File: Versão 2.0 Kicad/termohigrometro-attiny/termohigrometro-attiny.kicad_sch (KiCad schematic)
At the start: 19 parts, among them J1 Conn_02x03_Odd_Even, J3 Chave, J4 Screw_Terminal_01x04, J5 Screw_Terminal_01x04, J6 Carregador, U1 ATtiny85-20P, U2 AMS1117-3.3

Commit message: placa com attiny
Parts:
- added J2: Fan, TerminalBlock_4Ucon:TerminalBlock_4Ucon_1x02_P3.50mm_Horizontal, symbol Connector:Screw_Terminal_01x02
- added Q1: 2N7002K, Package_TO_SOT_SMD:SOT-23, symbol Transistor_FET:2N7002K
- added R1, R4: 1M, Resistor_THT:R_Axial_DIN0207_L6.3mm_D2.5mm_P10.16mm_Horizontal, symbol Device:R
- added R6: 100, Resistor_THT:R_Axial_DIN0207_L6.3mm_D2.5mm_P10.16mm_Horizontal, symbol Device:R
- added R7: 10k, Resistor_SMD:R_0805_2012Metric, symbol Device:R
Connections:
- net +BATT: now also J2.1 (Pin_1), R1.1
- net GND: now also Q1.2 (S), R4.2, R7.1
- net FAN: now reaches U1.2 (XTAL1/PB3)
- net FAN: now also R6.1
- net VBS: now reaches U1.3 (XTAL2/PB4)
- net VBS: now also R1.2, R4.1
- new net: J2.2 (Pin_2), Q1.3 (D)
- new net: Q1.1 (G), R6.2, R7.2
- no-connect marks 2 -> 0
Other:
- note added: "https://mjvo.github.io/tutorials/circuits/attiny85/"
- moved on the sheet: BT1, C7, C8, J3, J6, U2

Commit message: organizando
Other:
- note added: "Bateria"
- note added: "Conectores I2C"
- note added: "Controlador Attiny85"
- note added: "Furos de montagem"
- note added: "Regulador de tensão"
- note added: "Saída a MOSFET"
- note added: "Sensor da bateria"
- company: (none) -> Sentium Controls
- title: (none) -> Termohigrômetro
- moved on the sheet: BT1, C2, C7, C8, C9, D1, H1, H2, H3, J1, J2, J3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

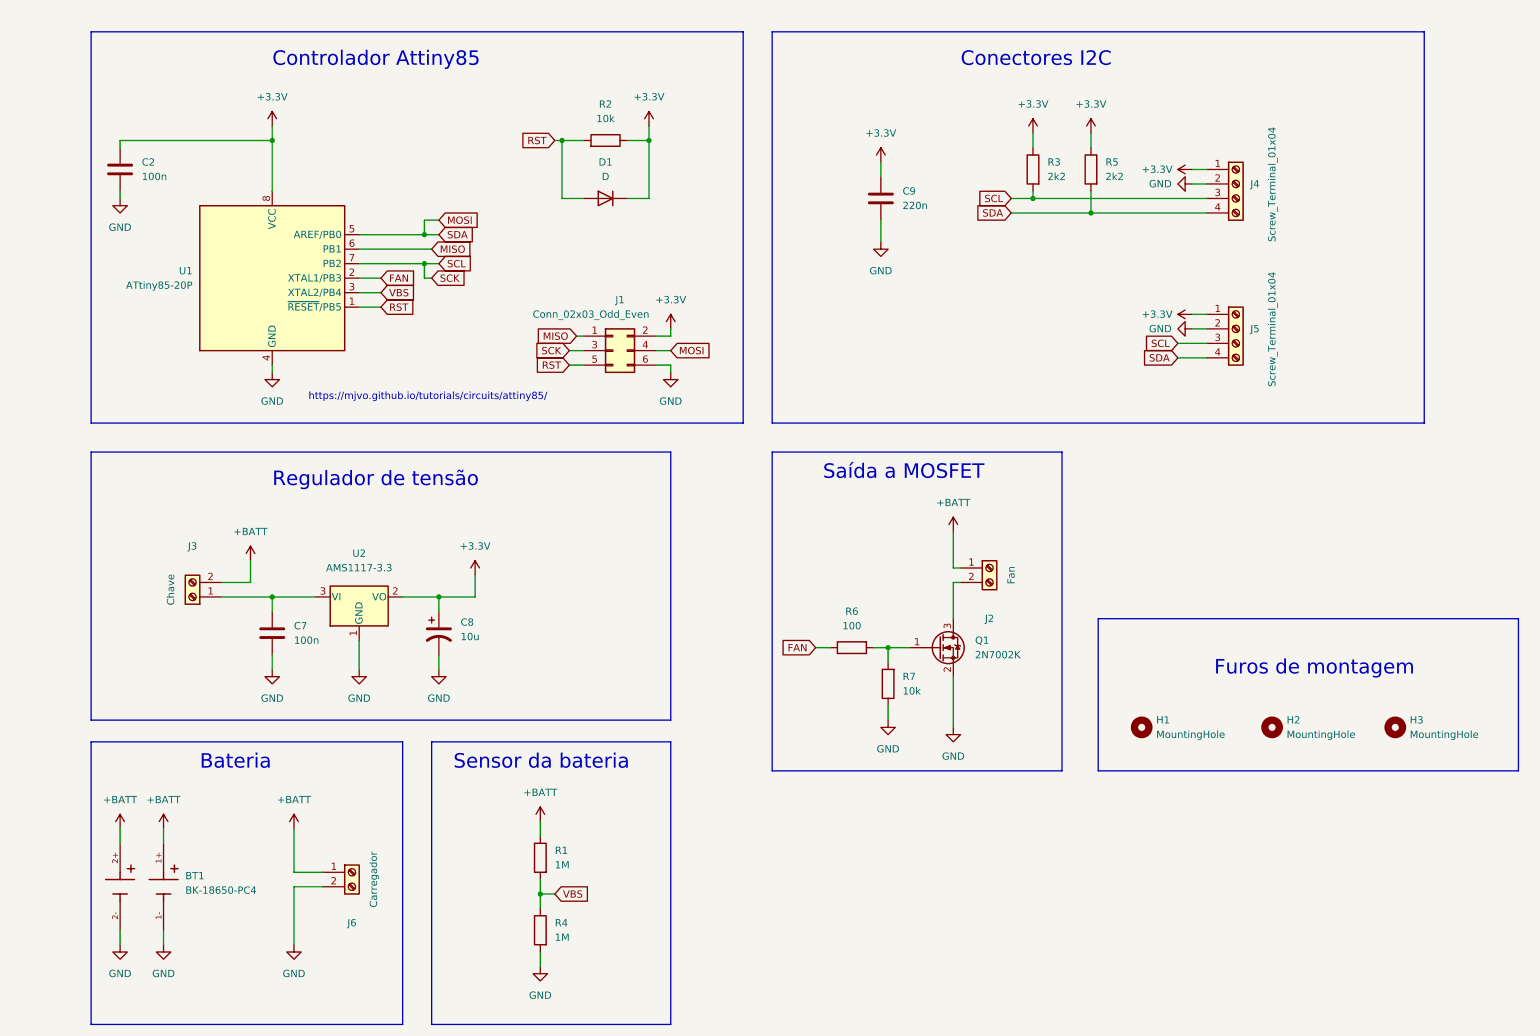
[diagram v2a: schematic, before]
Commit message: adicionado capacitor na leitura de tensão. Alterado ligação da bateria
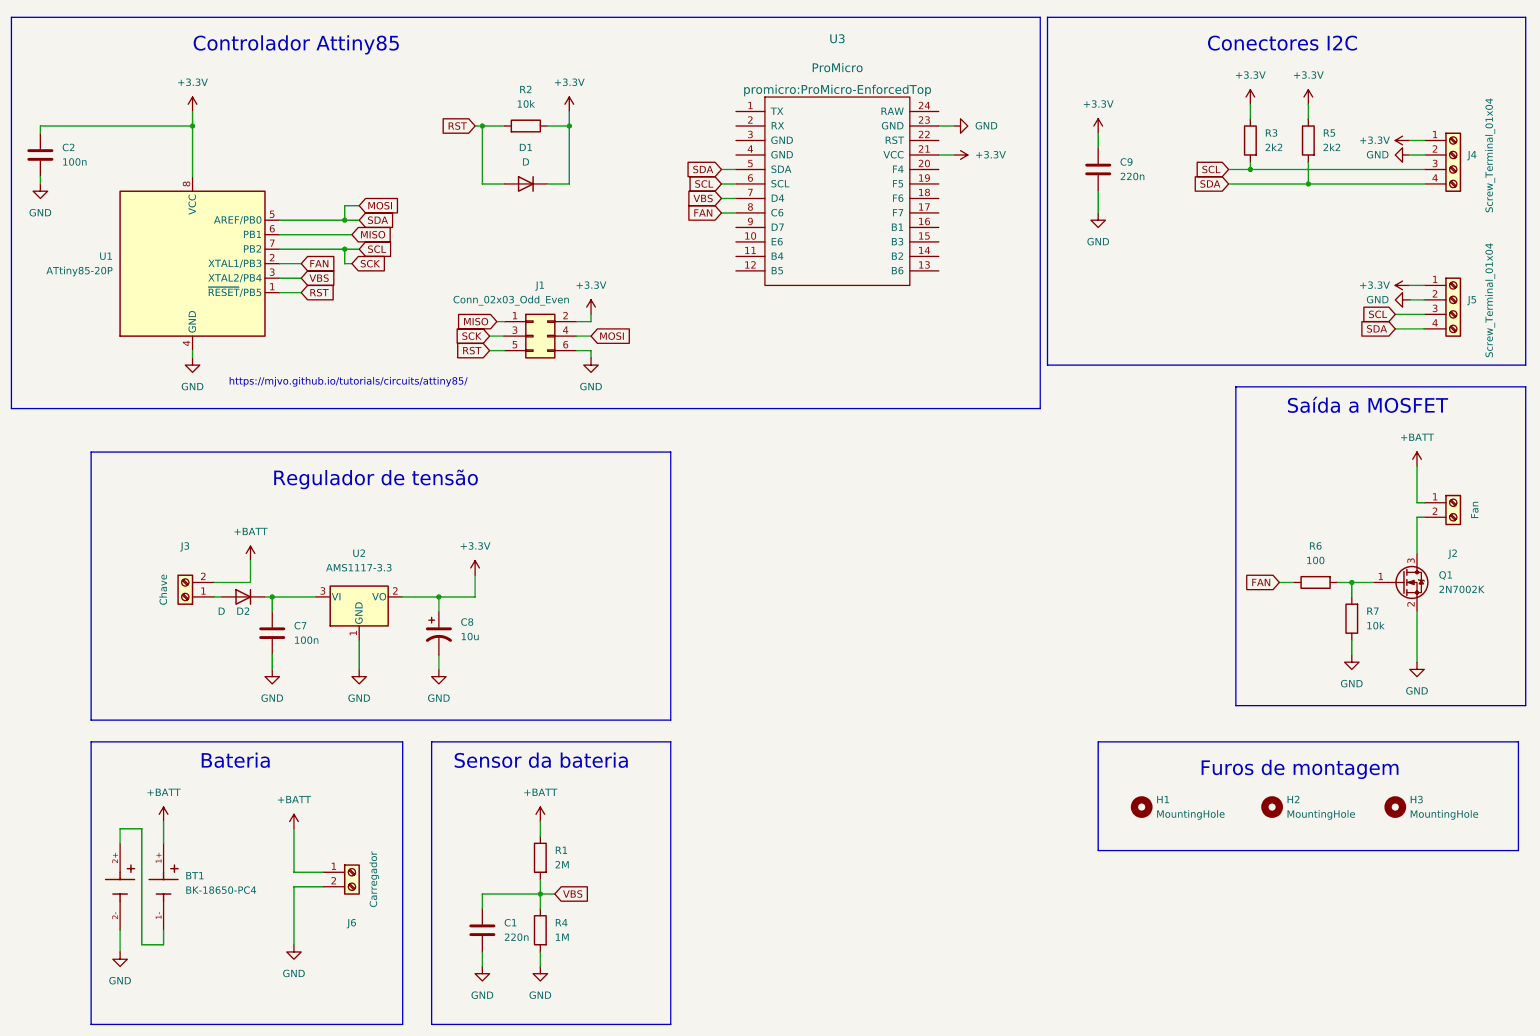
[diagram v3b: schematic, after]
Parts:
- added C1: 220n, Capacitor_THT:C_Disc_D5.0mm_W2.5mm_P5.00mm, symbol Device:C
- added D2: D, Diode_THT:D_DO-41_SOD81_P7.62mm_Horizontal, symbol Device:D
- added U3: ProMicro, promicro:ProMicro-EnforcedTop, symbol promicro:ProMicro
- R1: value 1M -> 2M
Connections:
- net +3V3: now also U3.21 (VCC)
- net +BATT: no longer BT1.2+
- net FAN: now also U3.8 (C6)
- net GND: now also C1.1, U3.23 (GND); no longer BT1.1-
- net MOSI: now also U3.5 (SDA)
- net SCK: now also U3.6 (SCL)
- net VBS: now also C1.2, U3.7 (D4)
- net at C7.2, U2.3 (VI): now also D2.1 (K); no longer J3.1 (Pin_1)
- new net: D2.2 (A), J3.1 (Pin_1)
- new net: BT1.1-, BT1.2+
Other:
- moved on the sheet: C2, C9, D1, H1, H2, H3, J1, J2, J3, J4, J5, Q1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
